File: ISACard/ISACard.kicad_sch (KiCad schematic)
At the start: 85 parts, among them J1 Bus_ISA_8bit, J2 ICSP, J3 EXTSPI, J4 SERCON, J5 Conn_01x16, Q1 2N3904, Q2 2N3906, SW1 SW_Push, U1 74LS86, U11 ATmega328P-P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

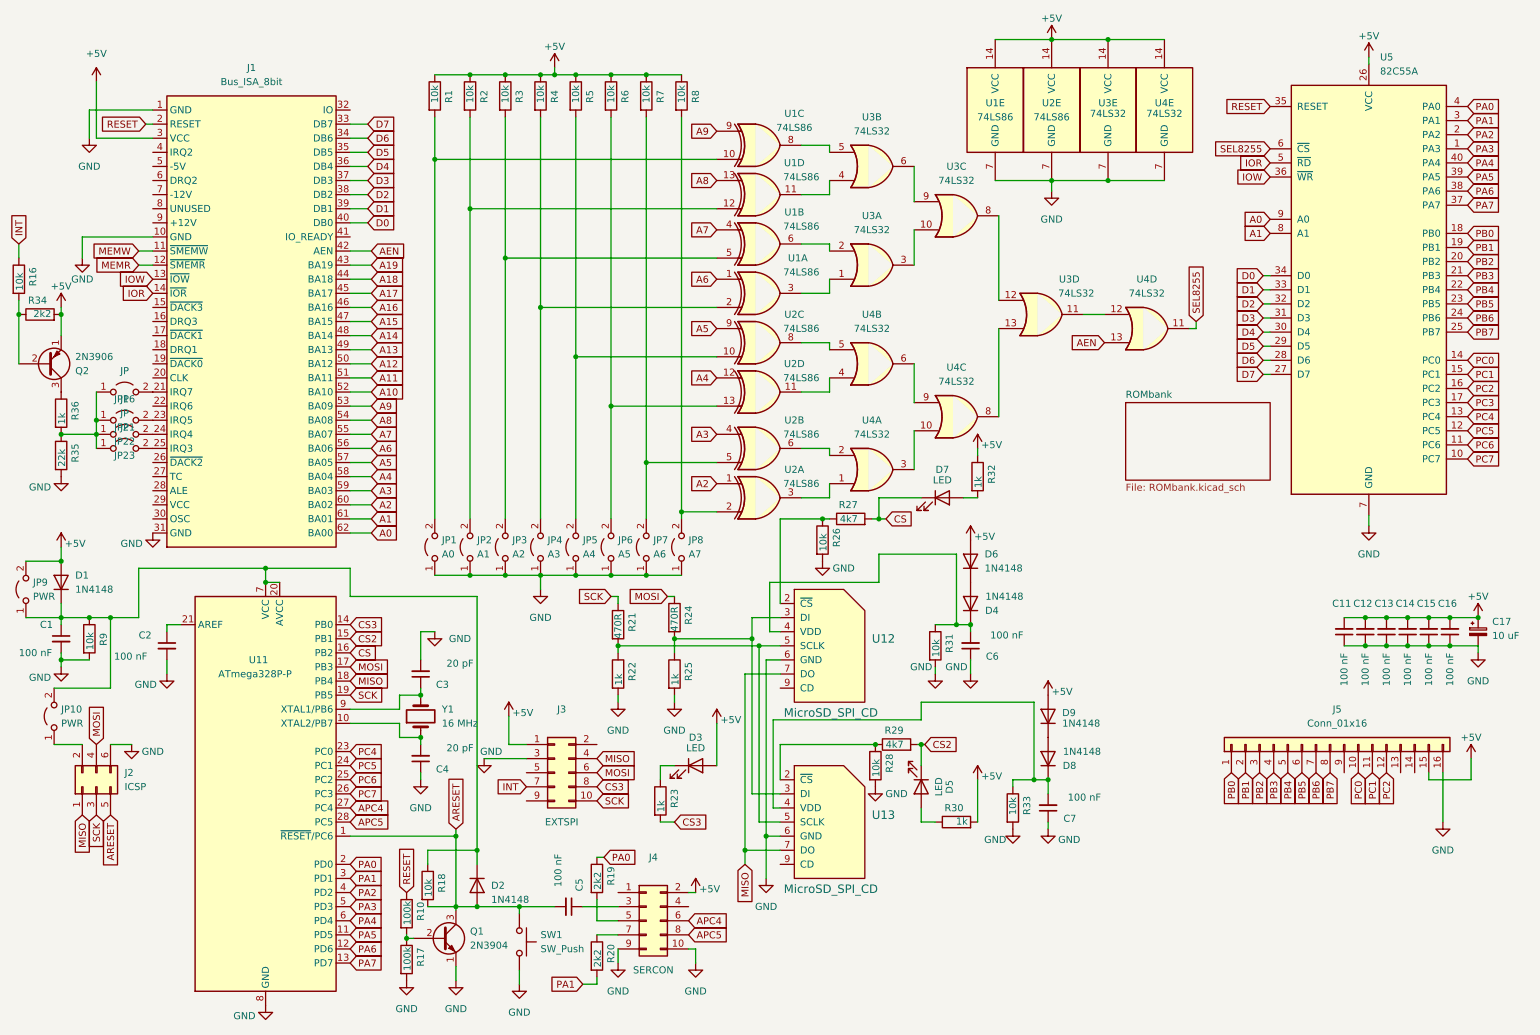
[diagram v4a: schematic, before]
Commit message: modified IRQ system
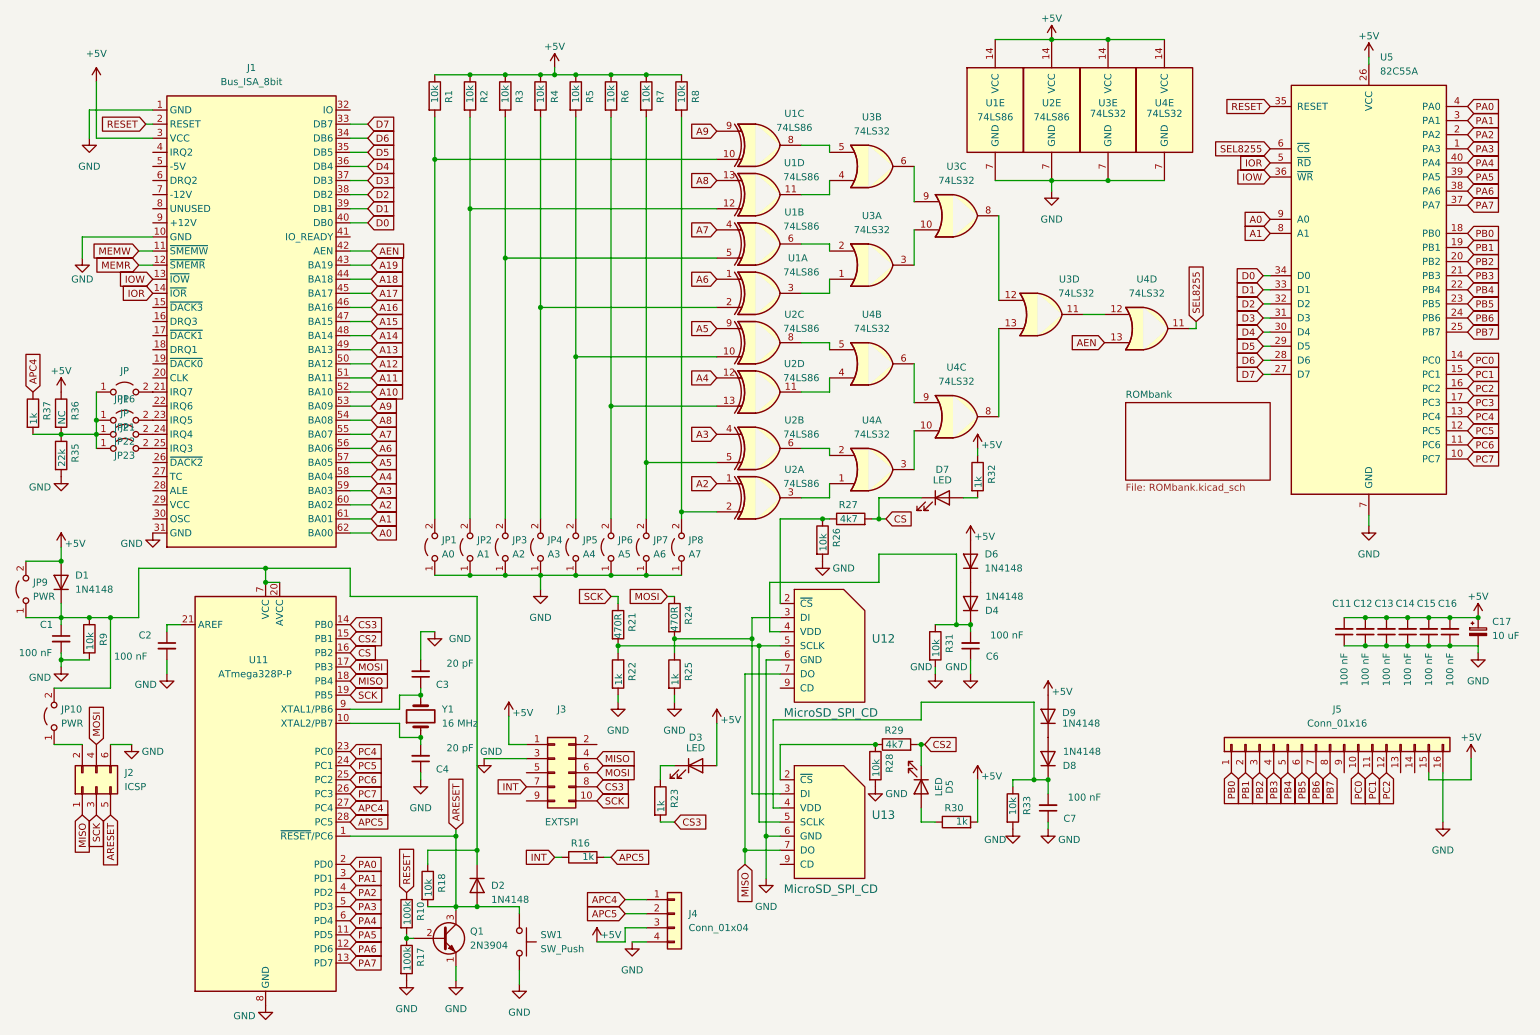
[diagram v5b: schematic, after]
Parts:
- removed C5: 100 nF, Capacitor_THT:C_Disc_D5.0mm_W2.5mm_P5.00mm, symbol Device:C_Small
- removed J4: SERCON, Connector_PinHeader_2.54mm:PinHeader_2x05_P2.54mm_Vertical, symbol Connector_Generic:Conn_02x05_Odd_Even
- removed Q2: 2N3906, Package_TO_SOT_THT:TO-92_Inline_Wide, symbol Transistor_BJT:2N3906
- removed R19, R20, R34: 2k2, Resistor_THT:R_Axial_DIN0207_L6.3mm_D2.5mm_P7.62mm_Horizontal, symbol Device:R
- added J4: Conn_01x04, Connector_PinHeader_2.54mm:PinHeader_1x04_P2.54mm_Vertical, symbol Connector_Generic:Conn_01x04
- added R37: 1k, Resistor_THT:R_Axial_DIN0207_L6.3mm_D2.5mm_P7.62mm_Horizontal, symbol Device:R
- R16: value 10k -> 1k
- R36: value 1k -> NC
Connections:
- net +5V: now also R36.1, J4.3 (Pin_3)
- net APC4: now also J4.1 (Pin_1), R37.1
- net APC5: now also R16.2, J4.2 (Pin_2)
- net GND: now also J4.4 (Pin_4)
- net at JP16.1 (A), JP21.1 (A), JP22.1 (A)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: now also R37.2

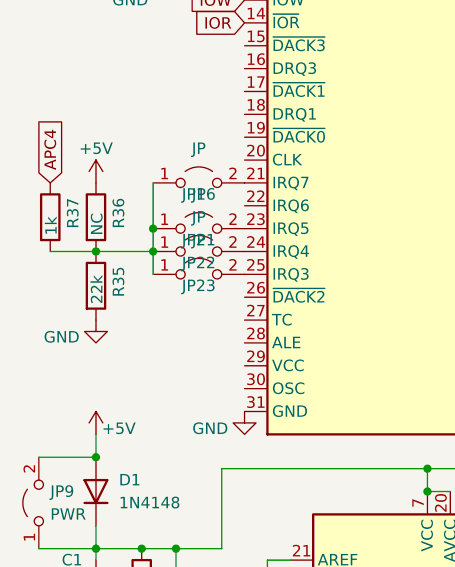
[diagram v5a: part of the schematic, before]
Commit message: Added IRQ response bit to determine spurious interrupt
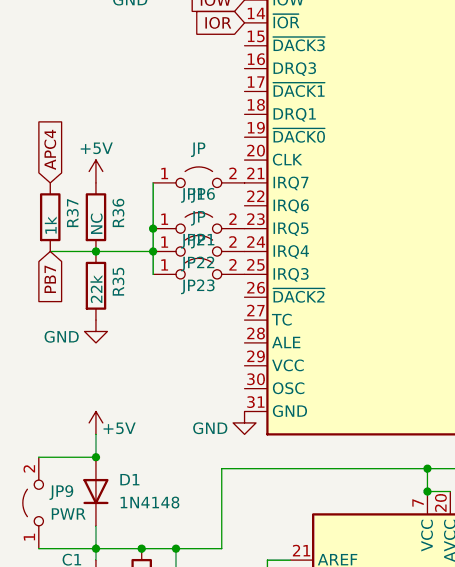
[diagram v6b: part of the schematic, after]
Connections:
- net PB7: now also JP16.1 (A), JP21.1 (A), JP22.1 (A), JP23.1 (A), R35.1, R36.2, R37.2
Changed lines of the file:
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@@
+    )
+  )
+  (global_label "PB7" (shape input) (at 16.51 91.44 270) (fields_autoplaced)
+    (effects (font (size 1.27 1.27)) (justify right))
+    (property "Intersheetrefs" "${INTERSHEET_REFS}" (at 16.4306 97.6026 90)
+      (effects (font (size 1.27 1.27)) (justify left) hide)
     )
   )

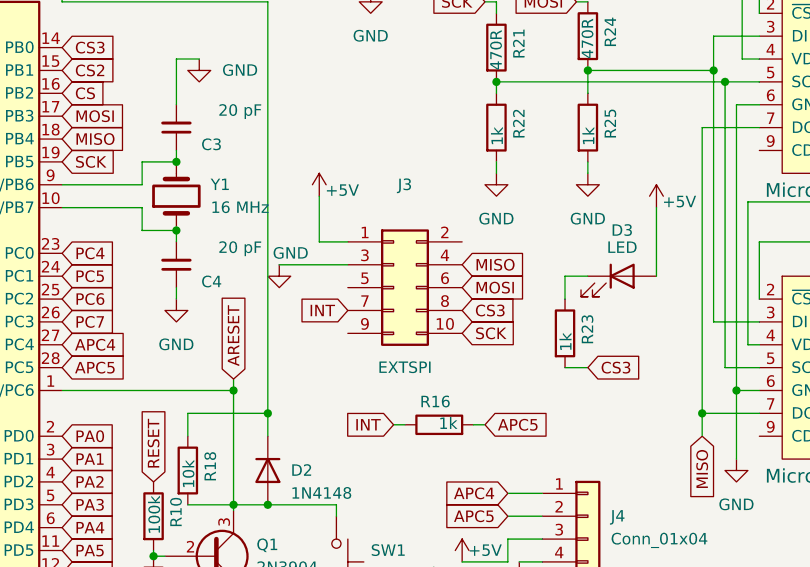
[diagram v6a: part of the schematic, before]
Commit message: ISACard modification
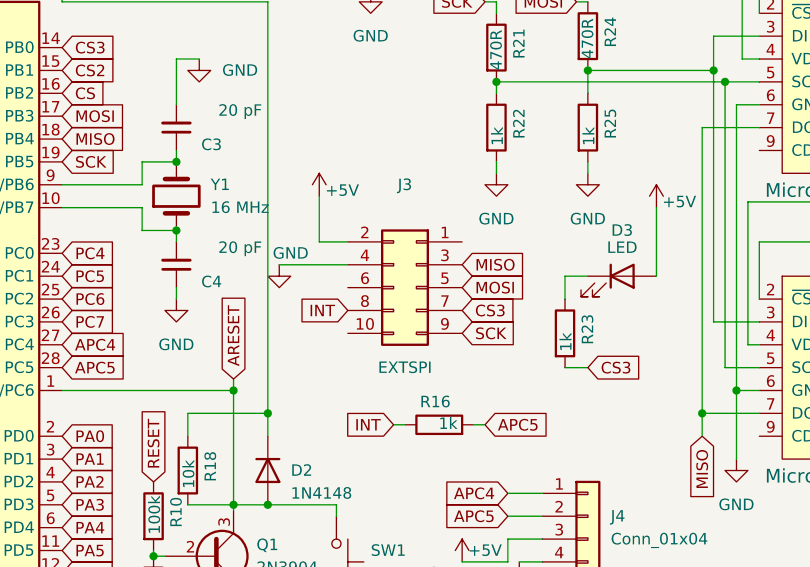
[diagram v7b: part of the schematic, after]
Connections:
- net +5V: now also J3.2 (Pin_2); no longer J3.1 (Pin_1)
- net CS3: now also J3.7 (Pin_7); no longer J3.8 (Pin_8)
- net GND: now also J3.4 (Pin_4); no longer J3.3 (Pin_3)
- net INT: now also J3.8 (Pin_8); no longer J3.7 (Pin_7)
- net MISO: now also J3.3 (Pin_3); no longer J3.4 (Pin_4)
- net MOSI: now also J3.5 (Pin_5); no longer J3.6 (Pin_6)
- net SCK: now also J3.9 (Pin_9); no longer J3.10 (Pin_10)
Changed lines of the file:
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@@
     (stroke (width 0) (type default))
   )
+  (wire (pts (xy 102.235 147.32) (xy 105.41 147.32))
+    (stroke (width 0) (type default))
+  )
   (wire (pts (xy 121.92 129.54) (xy 147.32 129.54))
     (stroke (width 0) (type default))
@@
     (stroke (width 0) (type default))
   )
-  (wire (pts (xy 102.235 147.32) (xy 105.41 147.32))
-    (stroke (width 0) (type default))
-  )
   (wire (pts (xy 199.39 153.67) (xy 196.85 153.67))
     (stroke (width 0) (type default))
@@
     )
   )
-  (symbol (lib_id "Connector_Generic:Conn_02x05_Odd_Even") (at 110.49 152.4 0) (unit 1)
+  (symbol (lib_id "Connector_Generic:Conn_02x05_Odd_Even") (at 113.03 152.4 0) (mirror y) (unit 1)
     (in_bom yes) (on_board yes) (dnp no)
     (property "Reference" "J3" (at 111.76 140.97 0)
@@
       (effects (font (size 1.27 1.27)))
     )
-    (property "Footprint" "Connector_PinHeader_2.54mm:PinHeader_2x05_P2.54mm_Vertical" (at 110.49 152.4 0)
+    (property "Footprint" "Connector_PinHeader_2.54mm:PinHeader_2x05_P2.54mm_Vertical" (at 113.03 152.4 0)
       (effects (font (size 1.27 1.27)) hide)
     )
-    (property "Datasheet" "~" (at 110.49 152.4 0)
+    (property "Datasheet" "~" (at 113.03 152.4 0)
       (effects (font (size 1.27 1.27)) hide)
     )
